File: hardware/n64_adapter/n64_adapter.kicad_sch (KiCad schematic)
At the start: 7 parts, among them J1 N64_Slot, J2 CART SLOT TOP ROW, J3 CART SLOT BOTTOM ROW, J4 Conn_01x01, J5 Conn_01x01, J6 Conn_01x01

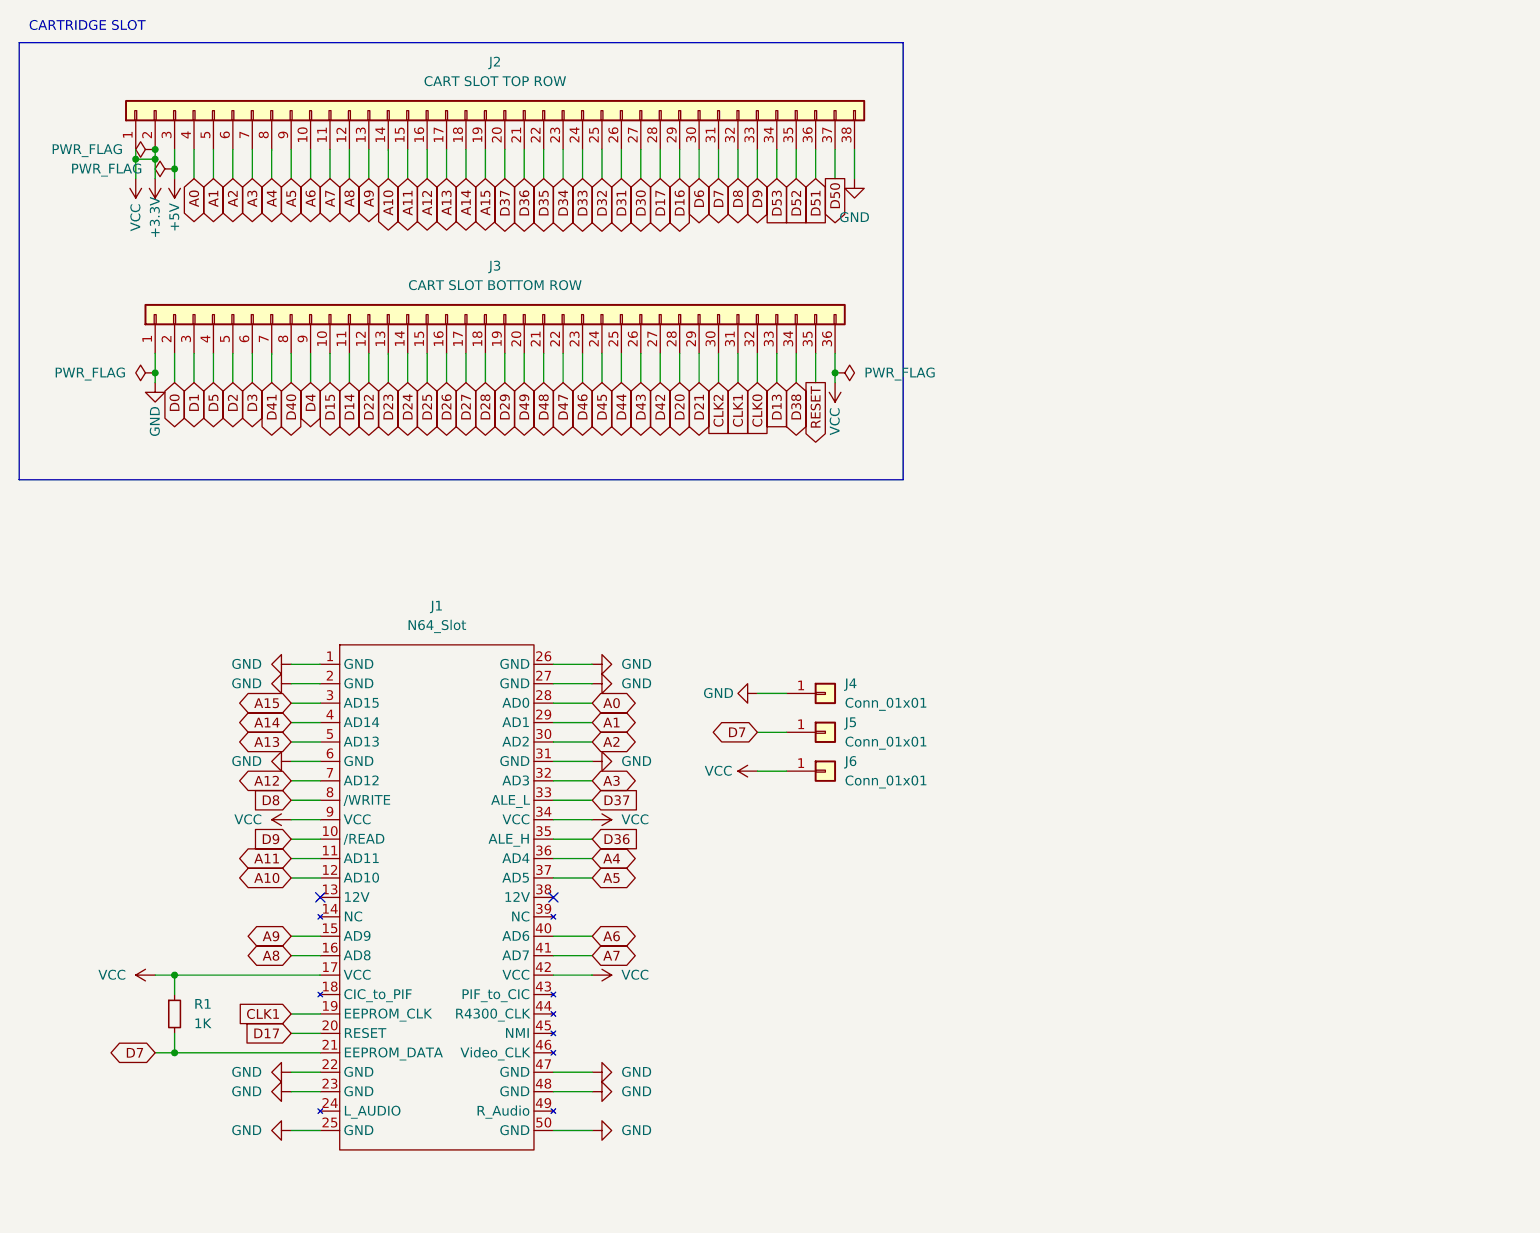
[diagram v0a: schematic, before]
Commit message: update n64 breakout
Propagate changes from main PCB to N64 breakout board
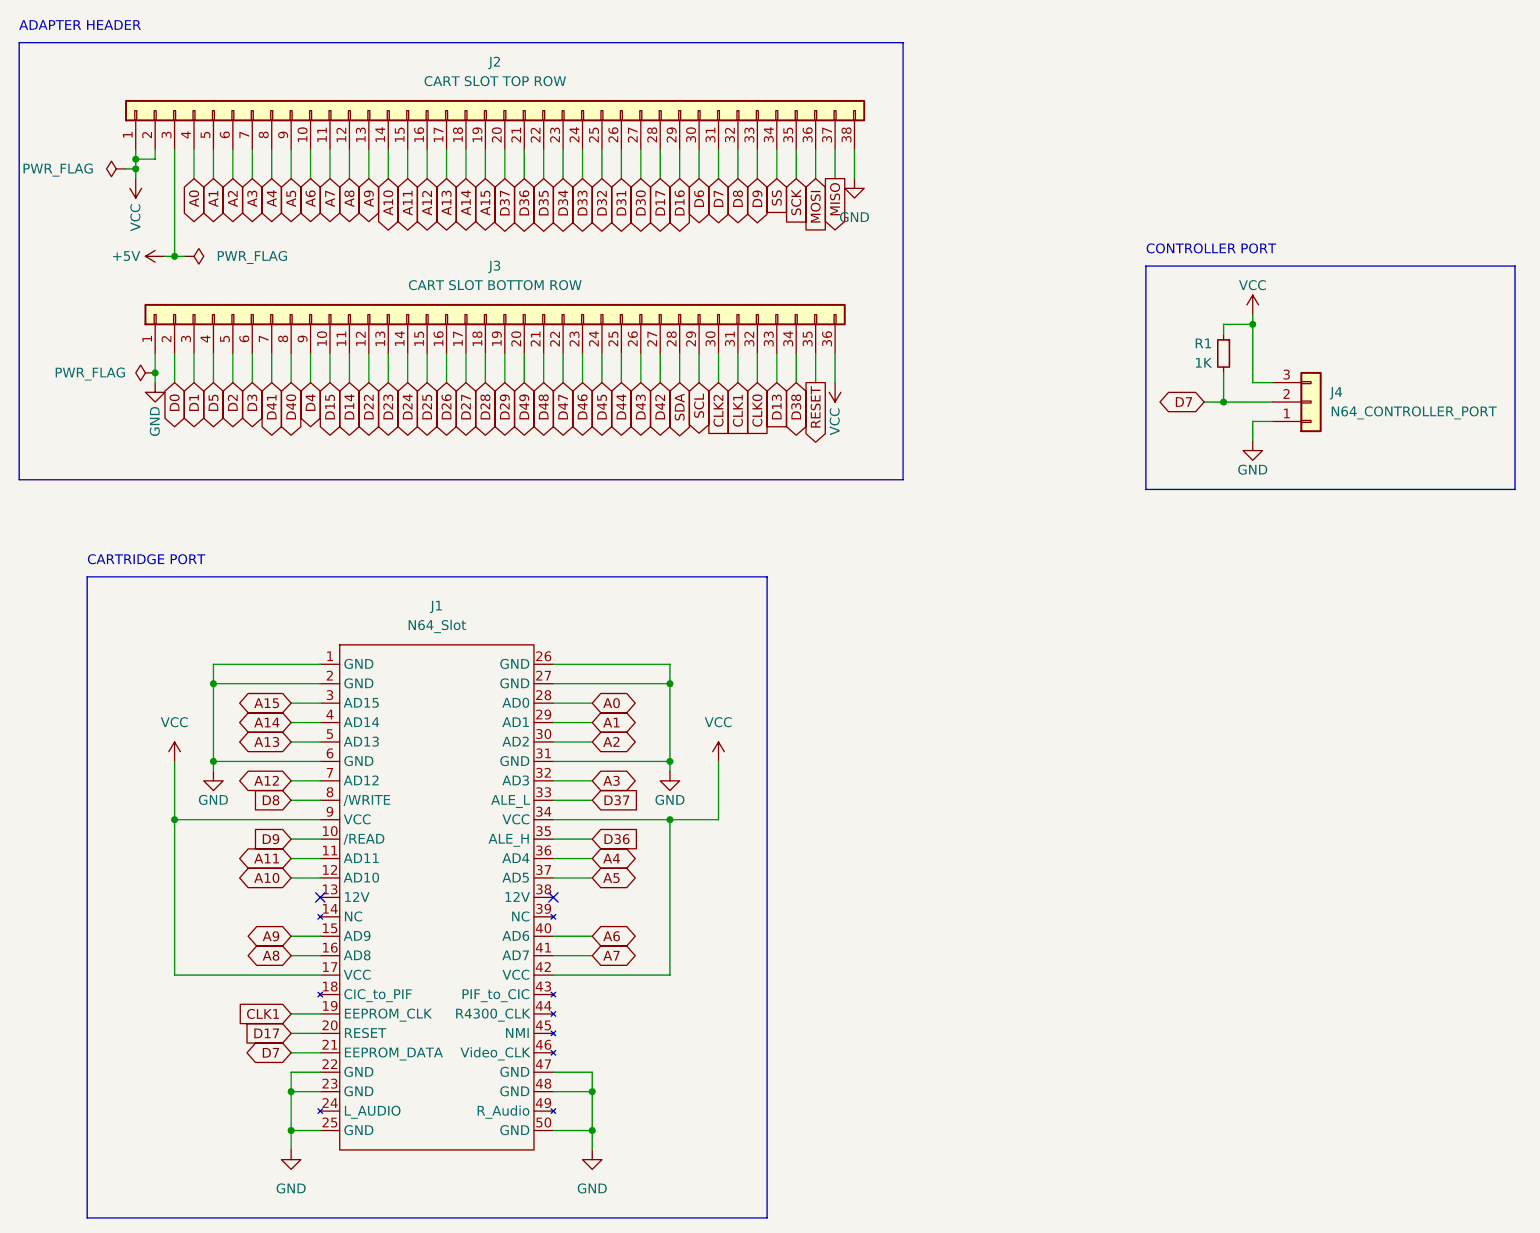
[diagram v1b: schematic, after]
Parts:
- removed J4, J5, J6: Conn_01x01, symbol Connector_Generic:Conn_01x01
- added J4: N64_CONTROLLER_PORT, symbol Connector_Generic:Conn_01x03
- J1: footprint (none) -> !OSCR:N64 Slot; symbol sanni:N64_Slot -> !OSCR:N64_Slot
- R1: footprint (none) -> Resistor_THT:R_Axial_DIN0207_L6.3mm_D2.5mm_P10.16mm_Horizontal
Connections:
- net D7: now also J4.2 (Pin_2)
- net GND: now also J4.1 (Pin_1)
- net +3V3 renamed VCC
- net VCC: now also J4.3 (Pin_3)
- net D20 renamed SDA
- net D21 renamed SCL
- net D50 renamed MISO
- net D51 renamed MOSI
- net D52 renamed SCK
- net D53 renamed SS
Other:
- note added: "ADAPTER HEADER"
- note added: "CARTRIDGE PORT"
- note added: "CONTROLLER PORT"
- note removed: "CARTRIDGE SLOT"
- title: OSCR N64 ADAPTER -> OSCR SHIELD - N64 BREAKOUT
- moved on the sheet: R1
